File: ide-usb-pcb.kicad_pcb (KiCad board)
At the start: 2 copper layers, 28 parts, among them J1 Conn_02x20_Odd_Even, J2 STM32F4_Discovery_Header, U1 TXS0108EPW, U2 TXS0108EPW

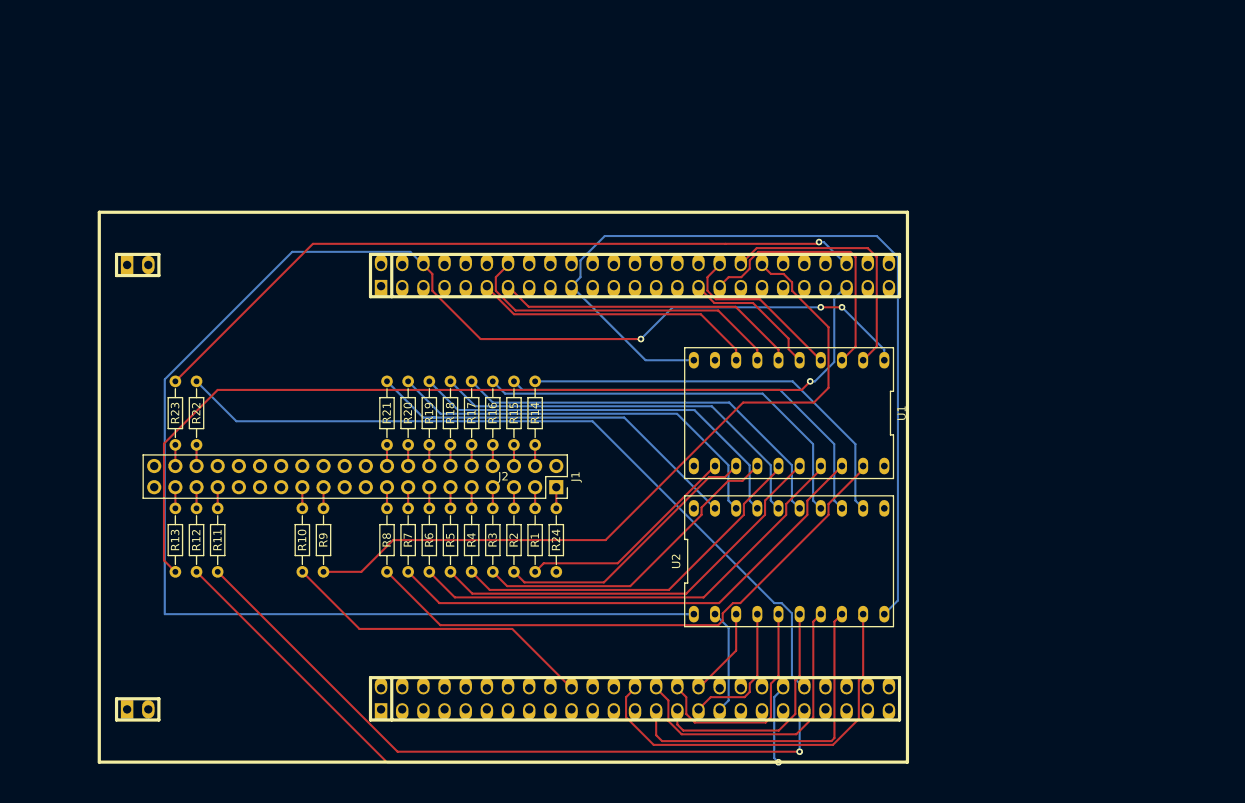
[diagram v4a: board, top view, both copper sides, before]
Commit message: Add ground plane and route missing traces
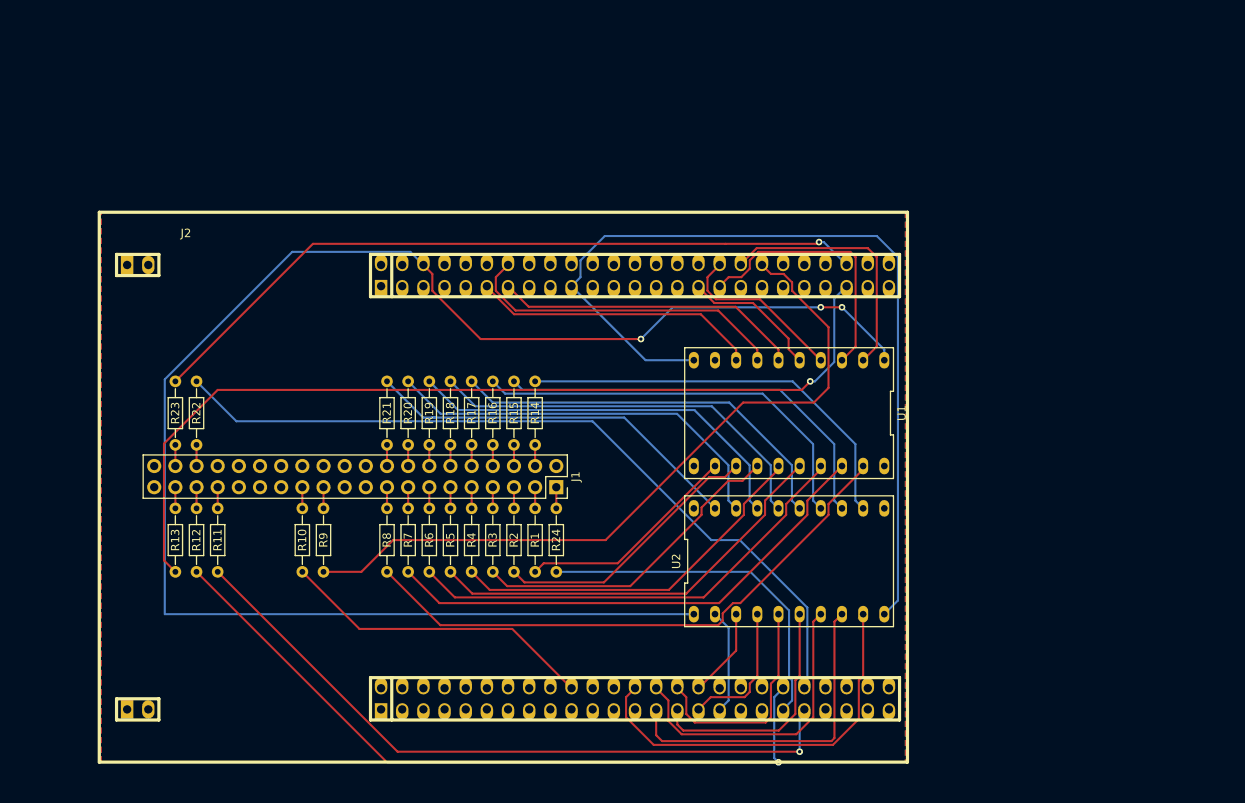
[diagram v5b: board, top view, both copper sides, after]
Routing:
- net /RESET: track 0.00 -> 42.3 mm
- net /DA2: track 92.6 -> 94.4 mm
- added copper zone on B.Cu, net GND
- added copper zone on F.Cu, net GND
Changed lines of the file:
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@@
     (thickness 1.6)
     (drawings 0)
-    (tracks 276)
+    (tracks 282)
     (zones 0)
     (modules 28)
@@
     (descr "STM32 F4 Discovery Header")
     (tags "STM32F4 Discovery")
-    (fp_text reference J2 (at 0 1.27) (layer F.SilkS)
+    (fp_text reference J2 (at 38.1 30.48) (layer F.SilkS)
       (effects (font (size 1.016 1.016) (thickness 0.2032)))
     )
@@
   (segment (start 120.65 100.89) (end 121.21 100.33) (width 0.25) (layer B.Cu) (net 55))
   (segment (start 120.65 105.41) (end 120.65 100.89) (width 0.25) (layer B.Cu) (net 55))
+  (segment (start 119.74501 99.25499) (end 118.67 100.33) (width 0.25) (layer B.Cu) (net 56))
+  (segment (start 119.74501 96.844717) (end 119.74501 99.25499) (width 0.25) (layer B.Cu) (net 56))
+  (segment (start 119.38 96.479707) (end 119.74501 96.844717) (width 0.25) (layer B.Cu) (net 56))
+  (segment (start 119.38 88.461839) (end 119.38 96.479707) (width 0.25) (layer B.Cu) (net 56))
+  (segment (start 114.738161 83.82) (end 119.38 88.461839) (width 0.25) (layer B.Cu) (net 56))
+  (segment (start 91.44 83.82) (end 114.738161 83.82) (width 0.25) (layer B.Cu) (net 56))
   (segment (start 86.15502 90.67502) (end 93.27 97.79) (width 0.25) (layer F.Cu) (net 57))
   (segment (start 67.81502 90.67502) (end 86.15502 90.67502) (width 0.25) (layer F.Cu) (net 57))
@@
   (segment (start 117.59499 106.16499) (end 117.59499 98.86501) (width 0.25) (layer B.Cu) (net 58))
   (segment (start 118.11 106.68) (end 117.59499 106.16499) (width 0.25) (layer B.Cu) (net 58))
-  (segment (start 119.72499 88.806829) (end 119.72499 96.30499) (width 0.25) (layer B.Cu) (net 59))
-  (segment (start 118.493151 87.57499) (end 119.72499 88.806829) (width 0.25) (layer B.Cu) (net 59))
-  (segment (start 117.616829 87.57499) (end 118.493151 87.57499) (width 0.25) (layer B.Cu) (net 59))
-  (segment (start 95.791889 65.75005) (end 117.616829 87.57499) (width 0.25) (layer B.Cu) (net 59))
-  (segment (start 53.05005 65.75005) (end 95.791889 65.75005) (width 0.25) (layer B.Cu) (net 59))
-  (segment (start 119.72499 96.30499) (end 121.21 97.79) (width 0.25) (layer B.Cu) (net 59))
-  (segment (start 48.26 60.96) (end 53.05005 65.75005) (width 0.25) (layer B.Cu) (net 59))
+  (segment (start 53.05005 65.75005) (end 48.26 60.96) (width 0.25) (layer B.Cu) (net 59))
+  (segment (start 95.791889 65.75005) (end 53.05005 65.75005) (width 0.25) (layer B.Cu) (net 59))
+  (segment (start 110.051839 80.01) (end 95.791889 65.75005) (width 0.25) (layer B.Cu) (net 59))
+  (segment (start 121.57501 88.116849) (end 113.468161 80.01) (width 0.25) (layer B.Cu) (net 59))
+  (segment (start 121.57501 97.42499) (end 121.57501 88.116849) (width 0.25) (layer B.Cu) (net 59))
+  (segment (start 113.468161 80.01) (end 110.051839 80.01) (width 0.25) (layer B.Cu) (net 59))
+  (segment (start 121.21 97.79) (end 121.57501 97.42499) (width 0.25) (layer B.Cu) (net 59))
   (segment (start 62.23 44.45) (end 111.76 44.45) (width 0.25) (layer F.Cu) (net 60))
   (segment (start 45.72 60.96) (end 62.23 44.45) (width 0.25) (layer F.Cu) (net 60))
@@
   (segment (start 50.8 73.66) (end 50.8 76.2) (width 0.25) (layer F.Cu) (net 67))
   (segment (start 91.44 76.2) (end 91.44 73.66) (width 0.25) (layer F.Cu) (net 68))
+  (zone (net 63) (net_name GND) (layer B.Cu) (hatch edge 0.508)
+    (connect_pads (clearance 0.508))
+    (min_thickness 0.254)
+    (fill yes (arc_segments 32) (thermal_gap 0.508) (thermal_bridge_width 0.508))
+    (polygon
+      (pts
+        (xy 133.35 106.68) (xy 36.83 106.68) (xy 36.83 40.64) (xy 133.35 40.64)
+      )
+    )
+  )
+  (zone (net 63) (net_name GND) (layer F.Cu) (hatch edge 0.508)
+    (connect_pads (clearance 0.508))
+    (min_thickness 0.254)
+    (fill yes (arc_segments 32) (thermal_gap 0.508) (thermal_bridge_width 0.508))
+    (polygon
+      (pts
+        (xy 133.35 106.68) (xy 36.83 106.68) (xy 36.83 40.64) (xy 133.35 40.64)
+      )
+    )
+  )
 )

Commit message: Yet another PCB design
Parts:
- moved R13 75.9 mm to (118.1, 99.1), turned to 0 degrees
- moved R12 72.7 mm to (118.1, 96.5), turned to 0 degrees
- moved R11 69.6 mm to (118.1, 94.0), turned to 0 degrees
- moved R23 66.6 mm to (100.3, 99.1), turned to 0 degrees
- moved R22 63.1 mm to (100.3, 96.5), turned to 0 degrees
- moved R10 57.7 mm to (118.1, 83.8), turned to 0 degrees
- moved R9 54.8 mm to (118.1, 81.3), turned to 0 degrees
- moved U1 54.7 mm to (68.6, 85.1), turned to 0 degrees
- moved U2 53.0 mm to (68.6, 67.3), turned to 180 degrees
- moved R24 35.1 mm to (118.1, 53.3), turned to 0 degrees
- moved R8 31.0 mm to (96.5, 94.0), turned to 180 degrees
- moved J1 30.6 mm to (114.3, 53.3), turned to 0 degrees
- moved R7 27.5 mm to (96.5, 91.4), turned to 180 degrees
- moved R6 24.0 mm to (96.5, 88.9), turned to 180 degrees
- moved R21 21.8 mm to (88.9, 73.7), turned to 0 degrees
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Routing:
- net +3V3: track 195.7 -> 0.00 mm, vias 3 -> 0
- net /OE: track 105.8 -> 0.00 mm
- net /DA0: track 88.9 -> 0.00 mm, vias 1 -> 0
- net /DIOW: track 88.7 -> 0.00 mm
- net /CS1: track 88.5 -> 0.00 mm, vias 1 -> 0
- net /DA1: track 84.1 -> 0.00 mm, vias 1 -> 0
- net /DD7A: track 0.00 -> 56.4 mm
- net /RESET: track 42.3 -> 81.9 mm
- net /DIOR: track 38.1 -> 0.00 mm
- net /DD0B: track 69.2 -> 35.5 mm
- net /DD15B: track 46.1 -> 12.5 mm
- net /DD14B: track 48.2 -> 15.0 mm
- net /DA2: track 94.4 -> 127.5 mm, vias 0 -> 1
- net /DD8A: track 48.1 -> 16.4 mm
- net /DD13B: track 48.2 -> 18.6 mm
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- removed copper zone on B.Cu, net GND
- removed copper zone on F.Cu, net GND

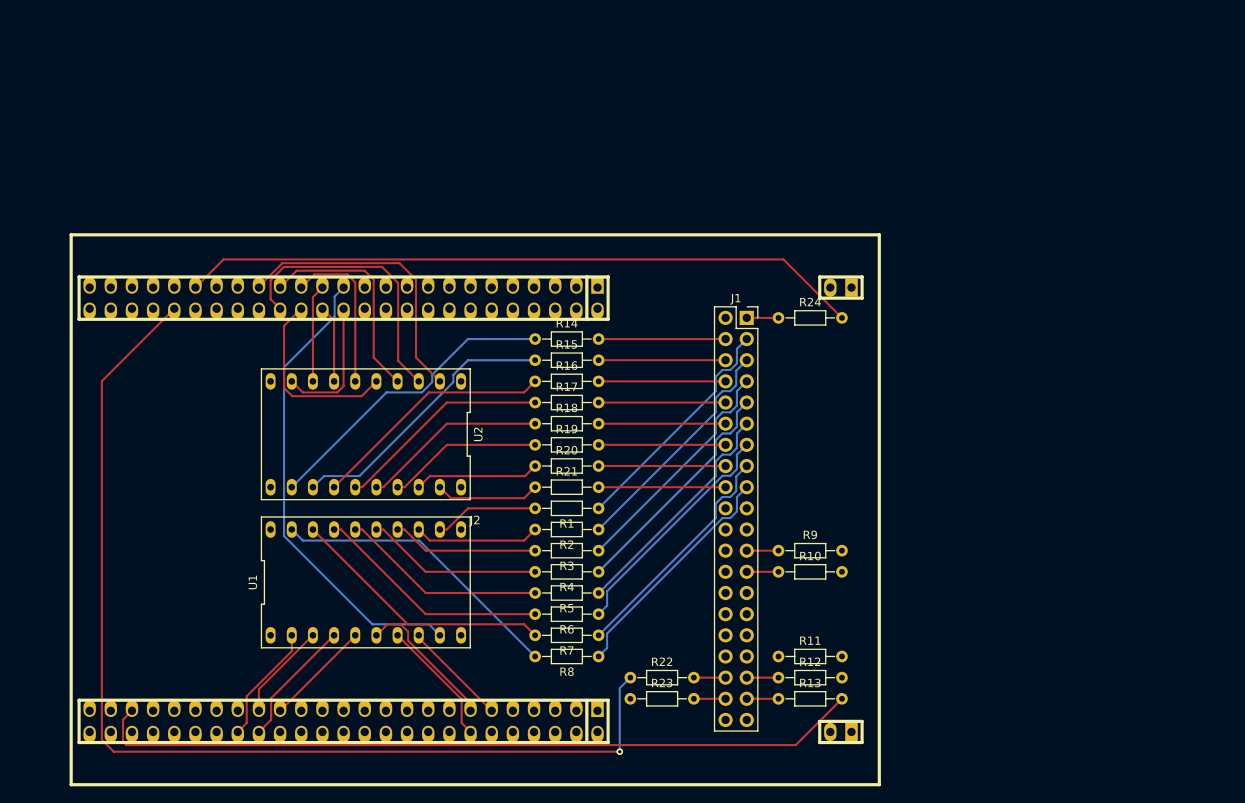
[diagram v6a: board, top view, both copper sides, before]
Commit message: Fix labels, route more traces
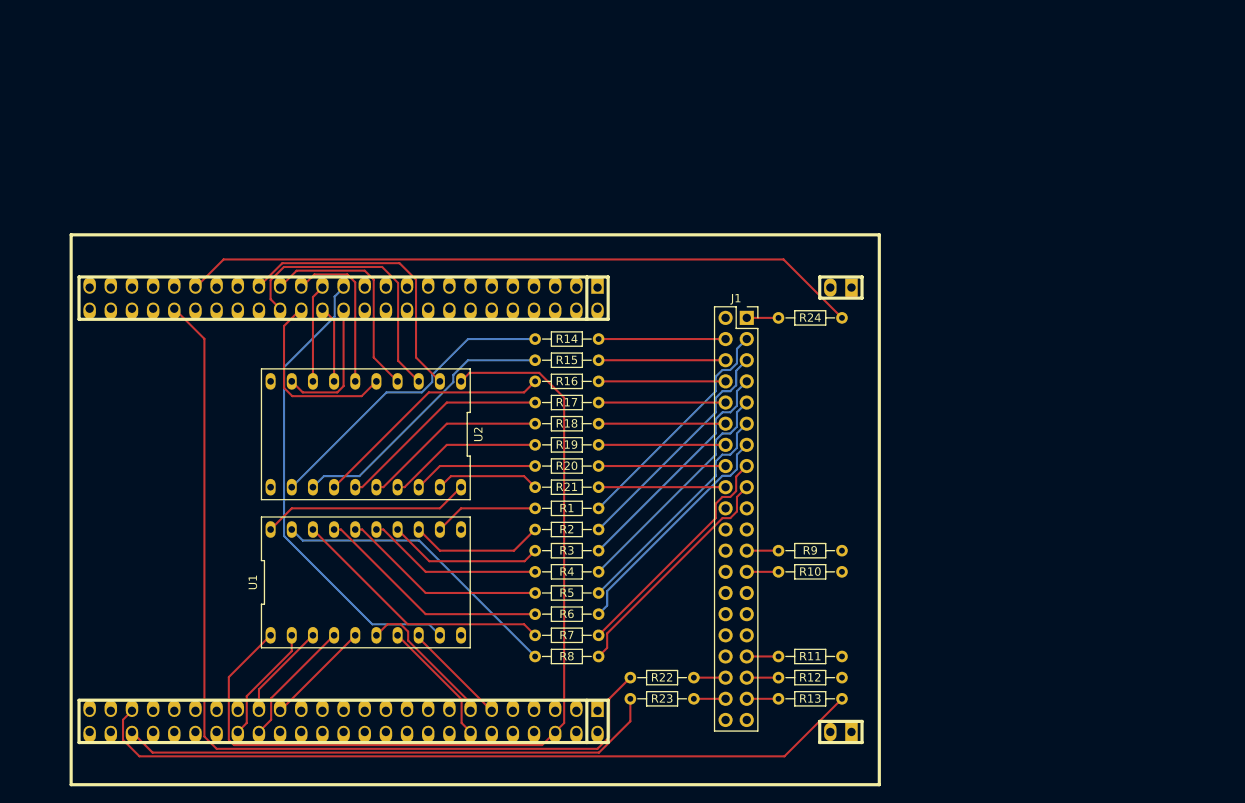
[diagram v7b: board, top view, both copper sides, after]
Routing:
- net +3V3: track 0.00 -> 109.3 mm
- net /CS1: track 0.00 -> 65.1 mm
- net +5V: track 0.00 -> 25.0 mm
- net /DA2: track 127.5 -> 110.8 mm, vias 1 -> 0
- net Net-(J1-Pad33): track 0.00 -> 3.81 mm
- net /DD5B: track 17.6 -> 18.6 mm
- net /DD6B: track 15.1 -> 16.1 mm
- net /CS0: track 92.9 -> 93.9 mm

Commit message: Add power connectors
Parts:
- added J3: Screw_Terminal_01x02, TerminalBlocks_Phoenix:TerminalBlock_Phoenix_MPT-2.54mm_2pol, F.Cu at (38.1, 77.5)
- added J4: USB_B, Connectors:USB_B, F.Cu at (36.8, 63.5)
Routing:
- net /DD7A: track 56.4 -> 27.6 mm
- net /DD15A: track 34.3 -> 16.3 mm
- net /DD14A: track 33.5 -> 19.4 mm
